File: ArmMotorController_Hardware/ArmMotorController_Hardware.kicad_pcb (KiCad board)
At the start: 2 copper layers, 98 parts, among them SW1 SW_Push, SW2 SW_Push, SW3 SW_Push, SW4 SW_Push, SW5 SW_SPDT, U1 AP1059, U2 AP1059, U3 TM4C129E_Launchpad, U4 MAX_3232, U5 VNH5019A_E, U6 VNH5019A_E, U7 VNH5019A_E, U8 VNH5019A_E

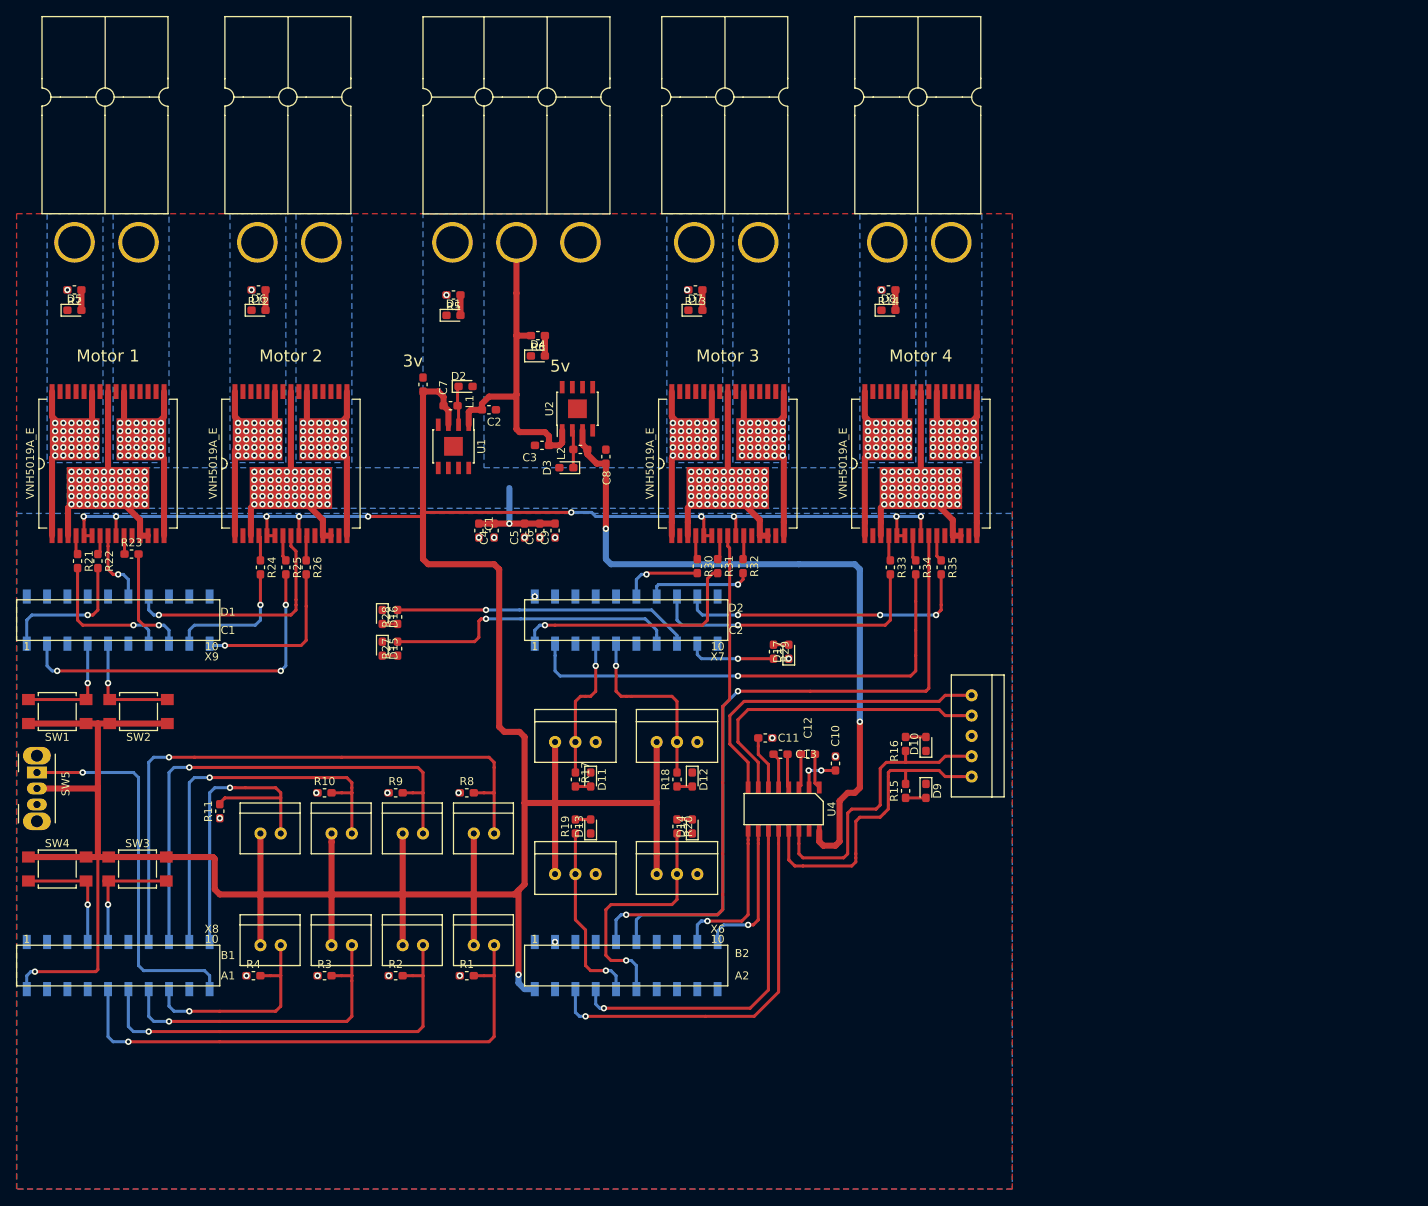
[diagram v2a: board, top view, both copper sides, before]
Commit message: added logo and signature at the bottom
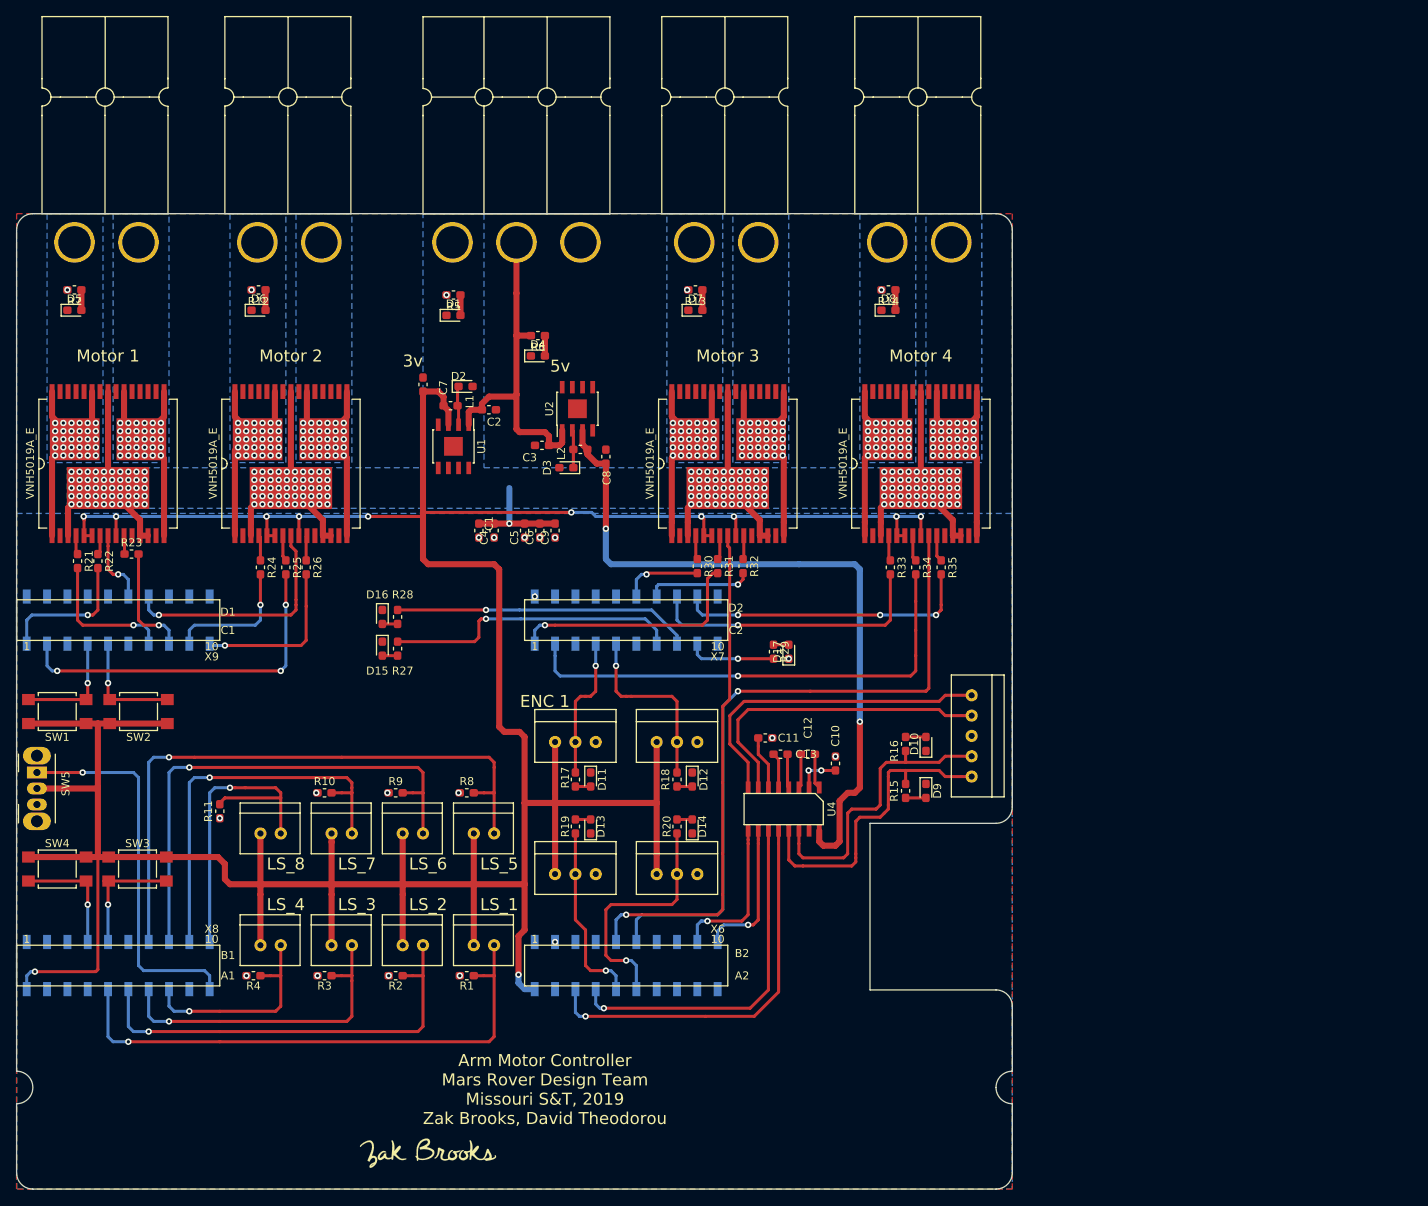
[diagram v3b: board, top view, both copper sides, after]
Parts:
- added G***: LOGO, MRDT_Silkscreens:Zak_Brooks_Sig_15mm, F.Cu at (90.4, 159.5)
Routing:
- net +3V3: track 459.7 -> 458.6 mm
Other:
- board outline added: 124.5 x 121.9 mm
- board text added: "Arm Motor Controller Mars Rover Design Team Missouri S&T, 2019 Zak Brooks, David Theodorou"
- board text added: "ENC 1"
- board text added: "LS_1"
- board text added: "LS_2"
- board text added: "LS_3"
- board text added: "LS_4"
- board text added: "LS_5"
- board text added: "LS_6"
- board text added: "LS_7"
- board text added: "LS_8"

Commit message: Added circuit requested by Andrew, generated netlist, read netlist
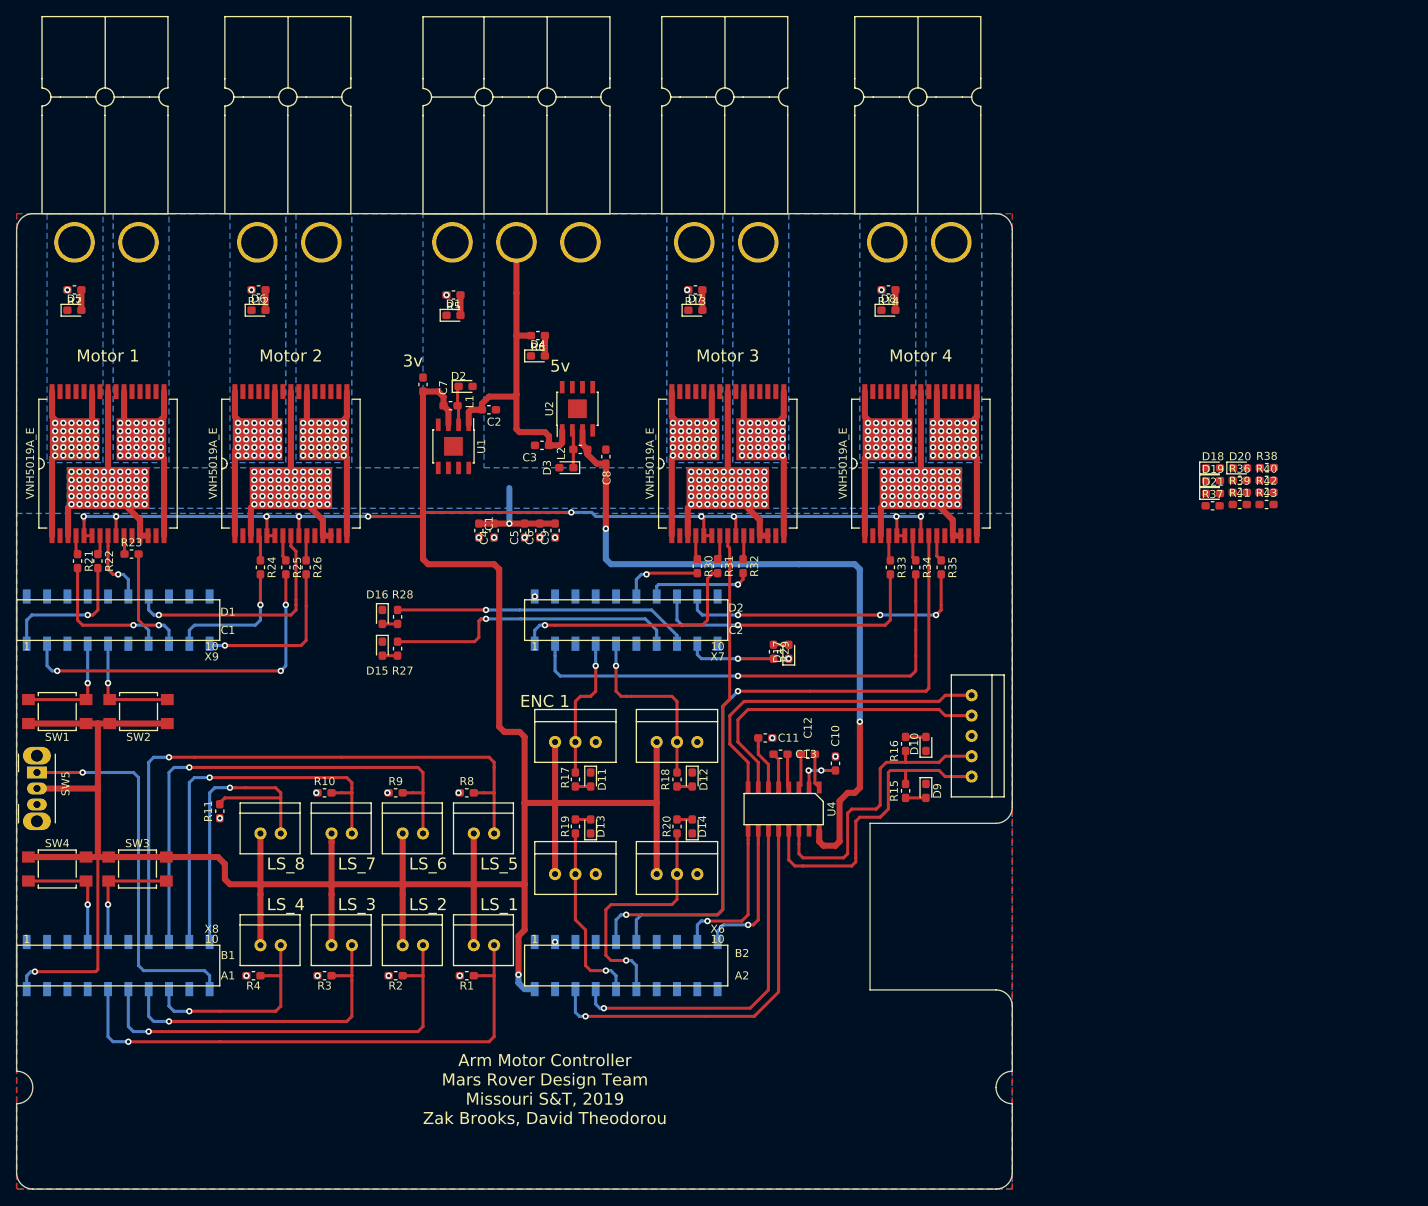
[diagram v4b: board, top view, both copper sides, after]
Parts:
- removed G***: LOGO, MRDT_Silkscreens:Zak_Brooks_Sig_15mm
- added D18: D_Schottky, Diode_SMD:D_0603_1608Metric_Pad1.05x0.95mm_HandSolder, F.Cu at (188.9, 73.7)
- added D19: D_Schottky, Diode_SMD:D_0603_1608Metric_Pad1.05x0.95mm_HandSolder, F.Cu at (188.9, 75.3)
- added D20: D_Schottky, Diode_SMD:D_0603_1608Metric_Pad1.05x0.95mm_HandSolder, F.Cu at (192.3, 73.7)
- added D21: D_Schottky, Diode_SMD:D_0603_1608Metric_Pad1.05x0.95mm_HandSolder, F.Cu at (188.9, 76.9)
- added R36: R, Resistor_SMD:R_0603_1608Metric_Pad1.05x0.95mm_HandSolder, F.Cu at (192.3, 75.2)
- added R37: R, Resistor_SMD:R_0603_1608Metric_Pad1.05x0.95mm_HandSolder, F.Cu at (188.9, 78.4)
- added R38: R, Resistor_SMD:R_0603_1608Metric_Pad1.05x0.95mm_HandSolder, F.Cu at (195.7, 73.7)
- added R39: R, Resistor_SMD:R_0603_1608Metric_Pad1.05x0.95mm_HandSolder, F.Cu at (192.3, 76.8)
- added R40: R, Resistor_SMD:R_0603_1608Metric_Pad1.05x0.95mm_HandSolder, F.Cu at (195.6, 75.2)
- added R41: R, Resistor_SMD:R_0603_1608Metric_Pad1.05x0.95mm_HandSolder, F.Cu at (192.3, 78.3)
- added R42: R, Resistor_SMD:R_0603_1608Metric_Pad1.05x0.95mm_HandSolder, F.Cu at (195.6, 76.8)
- added R43: R, Resistor_SMD:R_0603_1608Metric_Pad1.05x0.95mm_HandSolder, F.Cu at (195.6, 78.3)
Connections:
- U5 pad 6: +3V3 -> Net-(U5-Pad6)
- U5 pad 8: I_Sense_1 -> Net-(R38-Pad1)
- U6 pad 6: +3V3 -> Net-(U6-Pad6)
- U6 pad 8: I_Sense_2 -> Net-(R39-Pad1)
- U7 pad 6: +3V3 -> Net-(U7-Pad6)
- U7 pad 8: I_Sense_3 -> Net-(R42-Pad1)
- U8 pad 6: +3V3 -> Net-(U8-Pad6)
- U8 pad 8: +3V3 -> Net-(R43-Pad1)
- U8 pad 9: I_Sense_4 -> +3V3

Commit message: nothing worth noting
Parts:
- moved D21 23.6 mm to (212.1, 72.4)
- moved R41 19.2 mm to (211.2, 74.9)
- moved R43 17.7 mm to (211.2, 69.8)
- moved D20 15.2 mm to (207.4, 72.4)
- moved R37 13.9 mm to (202.3, 74.9)
- moved D19 13.3 mm to (201.9, 72.4)
- moved R42 13.3 mm to (207.0, 69.8)
- moved R39 12.2 mm to (202.3, 69.8)
- moved R40 11.8 mm to (207.4, 74.9)
- moved D18 8.43 mm to (197.2, 72.4)
- moved R36 4.60 mm to (196.8, 74.9)
- moved R38 4.12 mm to (197.2, 69.8)
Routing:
- net +3V3: track 458.6 -> 454.6 mm
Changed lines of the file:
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@@
     (thickness 1.6)
     (drawings 36)
-    (tracks 1211)
+    (tracks 1207)
     (zones 0)
     (modules 110)
@@
     (pad_to_mask_clearance 0.2)
     (aux_axis_origin 0 0)
-    (visible_elements 7FFFF7FF)
+    (visible_elements 7FFFFFFF)
     (pcbplotparams
       (layerselection 0x010fc_ffffffff)
@@
   )
   (module Diode_SMD:D_0603_1608Metric_Pad1.05x0.95mm_HandSolder (layer F.Cu)
-    (at 188.918001 73.693001)
+    (at 197.245 72.39)
     (descr "Diode SMD 0603 (1608 Metric), square (rectangular) end terminal, IPC_7351 nominal, (Body size source: http://www.tortai-tech.com/upload/download/2011102023233369053.pdf), generated with kicad-footprint-generator")
     (tags "diode handsolder")
@@
   )
   (module Diode_SMD:D_0603_1608Metric_Pad1.05x0.95mm_HandSolder (layer F.Cu)
-    (at 188.918001 75.283001)
+    (at 201.93 72.39)
     (descr "Diode SMD 0603 (1608 Metric), square (rectangular) end terminal, IPC_7351 nominal, (Body size source: http://www.tortai-tech.com/upload/download/2011102023233369053.pdf), generated with kicad-footprint-generator")
     (tags "diode handsolder")
@@
   )
   (module Diode_SMD:D_0603_1608Metric_Pad1.05x0.95mm_HandSolder (layer F.Cu)
-    (at 192.308001 73.693001)
+    (at 207.405 72.39)
     (descr "Diode SMD 0603 (1608 Metric), square (rectangular) end terminal, IPC_7351 nominal, (Body size source: http://www.tortai-tech.com/upload/download/2011102023233369053.pdf), generated with kicad-footprint-generator")
     (tags "diode handsolder")
@@
   )
   (module Diode_SMD:D_0603_1608Metric_Pad1.05x0.95mm_HandSolder (layer F.Cu)
-    (at 188.918001 76.873001)
+    (at 212.09 72.39)
     (descr "Diode SMD 0603 (1608 Metric), square (rectangular) end terminal, IPC_7351 nominal, (Body size source: http://www.tortai-tech.com/upload/download/2011102023233369053.pdf), generated with kicad-footprint-generator")
     (tags "diode handsolder")
@@
   )
   (module Resistor_SMD:R_0603_1608Metric_Pad1.05x0.95mm_HandSolder (layer F.Cu)
-    (at 192.263001 75.243001)
+    (at 196.85 74.93)
     (descr "Resistor SMD 0603 (1608 Metric), square (rectangular) end terminal, IPC_7351 nominal with elongated pad for handsoldering. (Body size source: http://www.tortai-tech.com/upload/download/2011102023233369053.pdf), generated with kicad-footprint-generator")
     (tags "resistor handsolder")
@@
   )
   (module Resistor_SMD:R_0603_1608Metric_Pad1.05x0.95mm_HandSolder (layer F.Cu)
-    (at 188.873001 78.423001)
+    (at 202.325 74.93)
     (descr "Resistor SMD 0603 (1608 Metric), square (rectangular) end terminal, IPC_7351 nominal with elongated pad for handsoldering. (Body size source: http://www.tortai-tech.com/upload/download/2011102023233369053.pdf), generated with kicad-footprint-generator")
     (tags "resistor handsolder")
@@
   )
   (module Resistor_SMD:R_0603_1608Metric_Pad1.05x0.95mm_HandSolder (layer F.Cu)
-    (at 195.653001 73.653001)
+    (at 197.245 69.85)
     (descr "Resistor SMD 0603 (1608 Metric), square (rectangular) end terminal, IPC_7351 nominal with elongated pad for handsoldering. (Body size source: http://www.tortai-tech.com/upload/download/2011102023233369053.pdf), generated with kicad-footprint-generator")
     (tags "resistor handsolder")
@@
   )
   (module Resistor_SMD:R_0603_1608Metric_Pad1.05x0.95mm_HandSolder (layer F.Cu)
-    (at 192.263001 76.753001)
+    (at 202.325 69.85)
     (descr "Resistor SMD 0603 (1608 Metric), square (rectangular) end terminal, IPC_7351 nominal with elongated pad for handsoldering. (Body size source: http://www.tortai-tech.com/upload/download/2011102023233369053.pdf), generated with kicad-footprint-generator")
     (tags "resistor handsolder")
@@
   )
   (module Resistor_SMD:R_0603_1608Metric_Pad1.05x0.95mm_HandSolder (layer F.Cu)
-    (at 195.613001 75.243001)
+    (at 207.405 74.93)
     (descr "Resistor SMD 0603 (1608 Metric), square (rectangular) end terminal, IPC_7351 nominal with elongated pad for handsoldering. (Body size source: http://www.tortai-tech.com/upload/download/2011102023233369053.pdf), generated with kicad-footprint-generator")
     (tags "resistor handsolder")
@@
   )
   (module Resistor_SMD:R_0603_1608Metric_Pad1.05x0.95mm_HandSolder (layer F.Cu)
-    (at 192.263001 78.263001)
+    (at 211.215 74.93)
     (descr "Resistor SMD 0603 (1608 Metric), square (rectangular) end terminal, IPC_7351 nominal with elongated pad for handsoldering. (Body size source: http://www.tortai-tech.com/upload/download/2011102023233369053.pdf), generated with kicad-footprint-generator")
     (tags "resistor handsolder")
@@
   )
   (module Resistor_SMD:R_0603_1608Metric_Pad1.05x0.95mm_HandSolder (layer F.Cu)
-    (at 195.613001 76.753001)
+    (at 207.01 69.85)
     (descr "Resistor SMD 0603 (1608 Metric), square (rectangular) end terminal, IPC_7351 nominal with elongated pad for handsoldering. (Body size source: http://www.tortai-tech.com/upload/download/2011102023233369053.pdf), generated with kicad-footprint-generator")
     (tags "resistor handsolder")
@@
   )
   (module Resistor_SMD:R_0603_1608Metric_Pad1.05x0.95mm_HandSolder (layer F.Cu)
-    (at 195.613001 78.263001)
+    (at 211.215 69.85)
     (descr "Resistor SMD 0603 (1608 Metric), square (rectangular) end terminal, IPC_7351 nominal with elongated pad for handsoldering. (Body size source: http://www.tortai-tech.com/upload/download/2011102023233369053.pdf), generated with kicad-footprint-generator")
     (tags "resistor handsolder")
@@
   (segment (start 71.628 79.756) (end 74.676 79.756) (width 0.381) (layer B.Cu) (net 66))
   (segment (start 74.676 79.756) (end 83.312 79.756) (width 0.381) (layer B.Cu) (net 66))
-  (segment (start 47.800001 82.1563) (end 48.799999 82.1563) (width 0.381) (layer F.Cu) (net 66))
   (segment (start 47.800001 82.1563) (end 47.800001 80.215999) (width 0.381) (layer F.Cu) (net 66))
   (via (at 51.816 79.756) (size 0.8) (drill 0.4) (layers F.Cu B.Cu) (net 66))
@@
   (segment (start 51.816 79.756) (end 70.612 79.756) (width 0.381) (layer B.Cu) (net 66))
   (segment (start 70.612 79.756) (end 71.628 79.756) (width 0.381) (layer B.Cu) (net 66))
-  (segment (start 70.660001 82.1563) (end 71.659999 82.1563) (width 0.381) (layer F.Cu) (net 66))
   (via (at 152.4 79.756) (size 0.8) (drill 0.4) (layers F.Cu B.Cu) (net 66))
   (segment (start 152.4 82.1563) (end 152.4 79.756) (width 0.381) (layer F.Cu) (net 66))
-  (segment (start 149.400001 82.1563) (end 150.399999 82.1563) (width 0.381) (layer F.Cu) (net 66))
   (via (at 149.352 79.756) (size 0.8) (drill 0.4) (layers F.Cu B.Cu) (net 66))
   (segment (start 149.400001 79.804001) (end 149.352 79.756) (width 0.381) (layer F.Cu) (net 66))
   (segment (start 149.400001 82.1563) (end 149.400001 79.804001) (width 0.381) (layer F.Cu) (net 66))
   (segment (start 152.4 79.756) (end 149.352 79.756) (width 0.381) (layer B.Cu) (net 66))
-  (segment (start 125.270001 82.1563) (end 126.269999 82.1563) (width 0.381) (layer F.Cu) (net 66))
   (via (at 129.032 79.756) (size 0.8) (drill 0.4) (layers F.Cu B.Cu) (net 66))
   (segment (start 129.270001 79.994001) (end 129.032 79.756) (width 0.381) (layer F.Cu) (net 66))
